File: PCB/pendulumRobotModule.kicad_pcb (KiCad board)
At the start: 2 copper layers, 33 x 100 mm, 27 parts, among them J1 Conn_01x02_Female, J2 conn_3x4, J3 Conn_01x02_Male, J4 Conn_01x04_Female, J5 conn_3x3, J7 Conn_01x04_Female, U1 ESP32-devKit, U2 MPU6050-breakout, U3 buckConverter-adj

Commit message: PCB updated to version 1.2: added RX pulldown resistor and 5V buffer capacitor (both optional). Added some markings for buck converter. Web interface now has a fancy option for logging data (plotTest.htm)
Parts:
- added C6: 470u, Capacitors_THT:CP_Radial_D6.3mm_P2.50mm, F.Cu at (104.1, 85.7)
- added J6: Conn_01x02_Male, mylib:pinHeader_2x1_5.08mm, F.Cu at (97.8, 128.9)
- added R8: 100k, Resistors_SMD:R_0805_HandSoldering, B.Cu at (104.1, 57.8)
- C3: value 10u -> 1u
- R7: value 10k -> 3k3
- moved F1 2.54 mm to (97.8, 125.7)
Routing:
- net /IBUS_RX: track 35.8 -> 43.1 mm, vias 1 -> 2
- net +24V: track 92.5 -> 95.8 mm
- net Net-(F1-Pad2): track 8.67 -> 6.13 mm
- net +5V: track 70.7 -> 71.6 mm, vias 1 -> 2
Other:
- board text added: "BalancingRobot V1.2"
- board text added: "February 2019 gitlab.com/kloppertje/BalancingRobot/ elexperiment.nl"
- board text added: "In"
- board text added: "Out"
- board text removed: "BalancingRobot V1.1"
- board text removed: "October 2018 gitlab.com/kloppertje/BalancingRobot/ elexperiment.nl"

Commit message: PCB v1.3 update. Added power switch, battery connector, and status LEDs.
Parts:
- added D1: LED, LED_THT:LED_D5.0mm, F.Cu at (89.5, 54.6)
- added D2: LED, LED_THT:LED_D5.0mm, F.Cu at (90.2, 109.2)
- added J8: Conn_01x02_Male, Connector_JST:JST_XH_S02B-XH-A-1_1x02_P2.50mm_Horizontal, F.Cu at (99.1, 116.8)
- added R10: 100k, Resistors_SMD:R_0805_HandSoldering, B.Cu at (90.2, 74.9)
- added R9: 100k, Resistors_SMD:R_0805_HandSoldering, B.Cu at (90.2, 72.4)
- added SW1: SW_SPDT, mylib:switch_slider_SPDT, F.Cu at (88.4, 99.1)
- moved REF** 27.8 mm to (89.5, 38.0)
- moved REF** 22.0 mm to (89.5, 128.0)
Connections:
- J3 pad 1: Net-(F1-Pad2) -> Net-(J3-Pad1)
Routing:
- net Net-(D2-Pad2): track 0.00 -> 38.7 mm, vias 0 -> 1
- net Net-(J3-Pad1): track 0.00 -> 29.2 mm
- net Net-(F1-Pad2): track 6.13 -> 26.0 mm
- net Net-(D1-Pad2): track 0.00 -> 15.5 mm, vias 0 -> 1
- net /IMU_SDA: track 65.3 -> 79.0 mm
- net Net-(R9-Pad1): track 0.00 -> 3.81 mm
- net Net-(R10-Pad1): track 0.00 -> 3.81 mm
- net GND: track 1.95 -> 3.75 mm
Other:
- board size 33 x 100 mm -> 40 x 100 mm
- board text added: "Aug 2022 gitlab.com/kloppertje/BalancingRobot/ elexperiment.nl"
- board text added: "BalancingRobot V1.3"
- board text removed: "BalancingRobot V1.2"
- board text removed: "February 2019 gitlab.com/kloppertje/BalancingRobot/ elexperiment.nl"

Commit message: Some slight updates to PCB, also updated readme for PCB
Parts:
- added C7: 10u 50V, Capacitor_SMD:C_1206_3216Metric, B.Cu at (110.7, 70.6)
- added C8: 22u 10V, Capacitor_SMD:C_0805_2012Metric, B.Cu at (104.6, 70.4)
- added U4: R-78E5.0-0.5, Converter_DCDC:Converter_DCDC_RECOM_R-78E-0.5_THT, F.Cu at (110.5, 74.2)
- C1, C3: footprint Capacitors_SMD:C_0805_HandSoldering -> Capacitor_SMD:C_0805_2012Metric
- C5: footprint Capacitors_SMD:C_0805_HandSoldering -> Capacitor_SMD:C_0805_2012Metric; moved to B.Cu
- D1, D2: footprint LED_THT:LED_D5.0mm -> mylib:LED_D5.0mm_Horizontal
- R1, R10, R2, R3, R4, R5, R6, R7, R8, R9: footprint Resistors_SMD:R_0805_HandSoldering -> Resistor_SMD:R_0805_2012Metric
- moved C3 4.60 mm to (111.3, 62.7)
- moved R5 4.60 mm to (111.3, 67.8)
- moved C1 4.60 mm to (104.6, 67.8)
- moved R1 4.60 mm to (104.6, 62.7)
- moved R6 4.60 mm to (111.3, 65.3)
- moved R2 4.60 mm to (104.6, 65.3)
- moved D1 2.92 mm to (92.5, 54.6)
- moved C5 2.29 mm to (114.0, 104.1)
- moved D2 2.29 mm to (92.5, 109.2)
- moved J8 0.51 mm to (99.6, 116.8)
- moved R8 0.46 mm to (104.6, 57.8)
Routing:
- net Net-(C1-Pad1): track 57.8 -> 65.7 mm, vias 5 -> 3
- net +24V: track 95.8 -> 103.1 mm, vias 3 -> 2
- net /IMU_SDA: track 79.0 -> 71.8 mm
- net +5V: track 71.6 -> 78.6 mm, vias 2 -> 0
- net /motADir: track 70.6 -> 77.4 mm
- net /motBStp: track 84.2 -> 89.7 mm
- net /IMU_SCL: track 71.8 -> 76.0 mm
- net /BATT_VOLT: track 12.7 -> 15.8 mm
- net /motBDir: track 89.6 -> 92.5 mm
- net /DAC1: track 18.5 -> 16.0 mm, vias 2 -> 0
- net Net-(J3-Pad1): track 29.2 -> 31.5 mm
- net GND: track 3.75 -> 1.82 mm, vias 1 -> 0
- net VCC: track 199.6 -> 200.7 mm, vias 4 -> 5
- net Net-(D1-Pad2): track 15.5 -> 16.6 mm, vias 1 -> 0
- net /IBUS_RX: track 43.1 -> 44.0 mm
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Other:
- board text added: "OFF"
- board text added: "ON"

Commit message: Some final touches on the PCB
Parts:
- moved R9 15.3 mm to (104.6, 77.5), turned to 0 degrees
- moved R10 15.3 mm to (104.6, 79.8), turned to 0 degrees
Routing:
- net Net-(D1-Pad2): track 16.6 -> 27.0 mm
- net Net-(R9-Pad1): track 3.81 -> 10.4 mm
- net Net-(R10-Pad1): track 3.81 -> 10.4 mm
- net /AUX1: track 58.2 -> 53.1 mm
- net /AUX4: track 68.6 -> 66.9 mm
- net /IMU_SDA: track 71.8 -> 70.4 mm
- net /AUX2: track 59.6 -> 58.2 mm
- net Net-(D2-Pad2): track 39.0 -> 40.0 mm, vias 0 -> 2
- net /DAC1: track 16.0 -> 15.6 mm, vias 0 -> 2
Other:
- board text added: "Actual happiness always looks pretty squalid in comparison with the overcompensations for misery. And, of course, stability isn't nearly so spectacular as instability. And being contented has none of the glamour of a good fight against misfortune, none of the picturesqueness of a struggle with temptation, or a fatal overthrow by passion or doubt. Happiness is never grand."
- board text added: "From: Brave new world, Aldous Huxley"

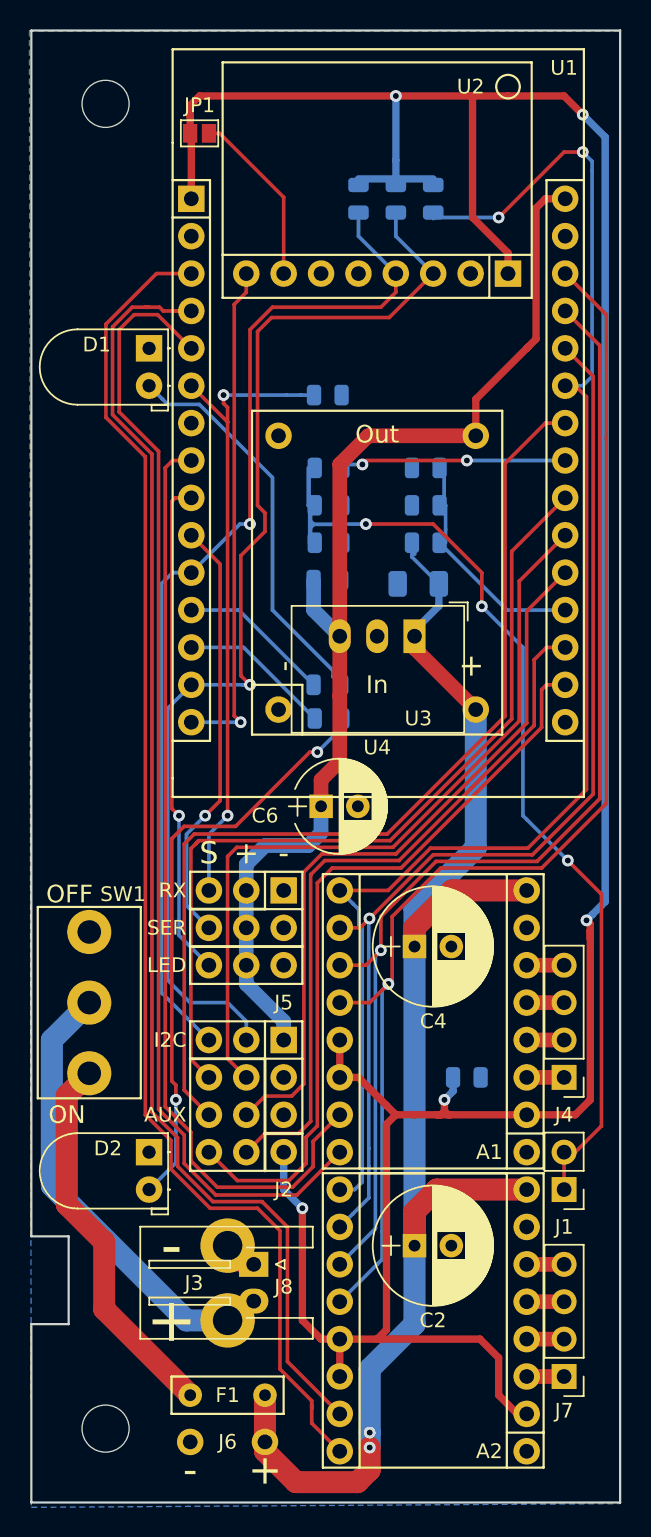
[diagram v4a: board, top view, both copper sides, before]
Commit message: Updated PCB design files to Kicad 7. Added cut-out for stepper motor cable pass-through. Updated PCB version to v1.4. Connected LEDS to gpio 33 and 26, as old connections were used for USB TX/RX.
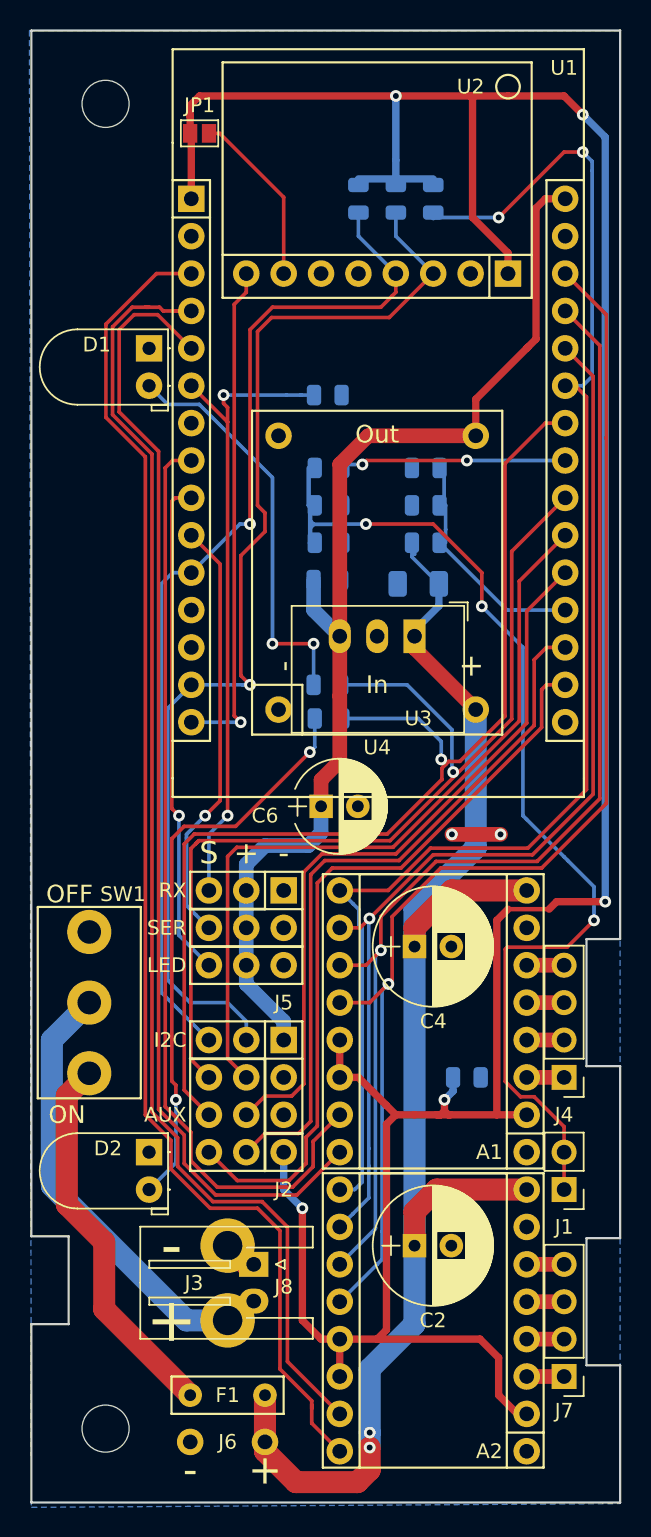
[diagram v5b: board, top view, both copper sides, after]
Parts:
- turned R10 to 180 degrees
- turned R9 to 180 degrees
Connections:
- R10 pad 1: Net-(R10-Pad1) -> /AUX4
- R9 pad 1: Net-(R9-Pad1) -> /AUX2
- SW1 pad 1: Net-(SW1-Pad1) -> unconnected-(SW1-A-Pad1)
- U1 pad 12: Net-(R9-Pad1) -> unconnected-(U1-GPIO3_/RX0-Pad12)
- U1 pad 13: Net-(R10-Pad1) -> unconnected-(U1-GPIO1_/TX0-Pad13)
- U1 pad 16: Net-(U1-Pad16) -> unconnected-(U1-EN-Pad16)
- U1 pad 7: Net-(U1-Pad7) -> unconnected-(U1-GPIO17/TX2-Pad7)
- U2 pad 5: Net-(U2-Pad5) -> unconnected-(U2-XDA-Pad5)
- U2 pad 6: Net-(U2-Pad6) -> unconnected-(U2-XCL-Pad6)
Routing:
- net /AUX2: track 58.2 -> 70.2 mm, vias 0 -> 1
- net Net-(R9-Pad1): track 10.4 -> 0.00 mm
- net Net-(R10-Pad1): track 10.4 -> 0.00 mm
- net /AUX4: track 66.9 -> 76.4 mm, vias 0 -> 1
- net Net-(J1-Pin_1): track 65.7 -> 71.0 mm
- net GND: track 1.82 -> 5.13 mm, vias 0 -> 2
- net VCC: track 200.7 -> 202.4 mm
- net Net-(D2-A): track 40.0 -> 38.9 mm
- net Net-(D1-A): track 27.0 -> 27.8 mm, vias 0 -> 2
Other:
- outline, holes or cut-outs redrawn
- net class Default removed
- net class lowPower removed
- net class power removed
- board text added: "Aug 2023 gitlab.com/kloppertje/BalancingRobot/ elexperiment.nl"
- board text added: "BalancingRobot V1.4"
- board text added: "From: Immortality, Milan Kundera"
- board text added: "However, when someone steps on my foot, only I feel the pain. The basis of the self is not thought but suffering, which is the most fundamental of all feelings. While it suffers, not even a cat can doubt its unique and uninterchangeable self. In intense suffering the world disappears and each of us is alone with his self. Suffering is the university of egocentrism."
- board text added: "I think, therefore I am is the statement of an intellectual who underrates toothaches. I feel, therefore I am is a truth much more universally valid, and it applies to everything that's alive."
- board text added: "My self does not differ substantially from yours in terms of its thought. Many people, few ideas: we all think more or less the same, and we exchange, borrow, steal thoughts from one another."
- board text removed: "Actual happiness always looks pretty squalid in comparison with the overcompensations for misery. And, of course, stability isn't nearly so spectacular as instability. And being contented has none of the glamour of a good fight against misfortune, none of the picturesqueness of a struggle with temptation, or a fatal overthrow by passion or doubt. Happiness is never grand."
- board text removed: "Aug 2022 gitlab.com/kloppertje/BalancingRobot/ elexperiment.nl"
- board text removed: "BalancingRobot V1.3"
- board text removed: "From: Brave new world, Aldous Huxley"
